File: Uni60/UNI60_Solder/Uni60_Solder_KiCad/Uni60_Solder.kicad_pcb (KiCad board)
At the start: 2 copper layers, 284.7 x 94.2 mm, 195 parts, among them J1 Conn_01x04, SW1 SW_Push, SW2 SW_Push, U1 STM32F072CBTx, U2 XC6206PxxxMR, U3 USBLC6-2SC6

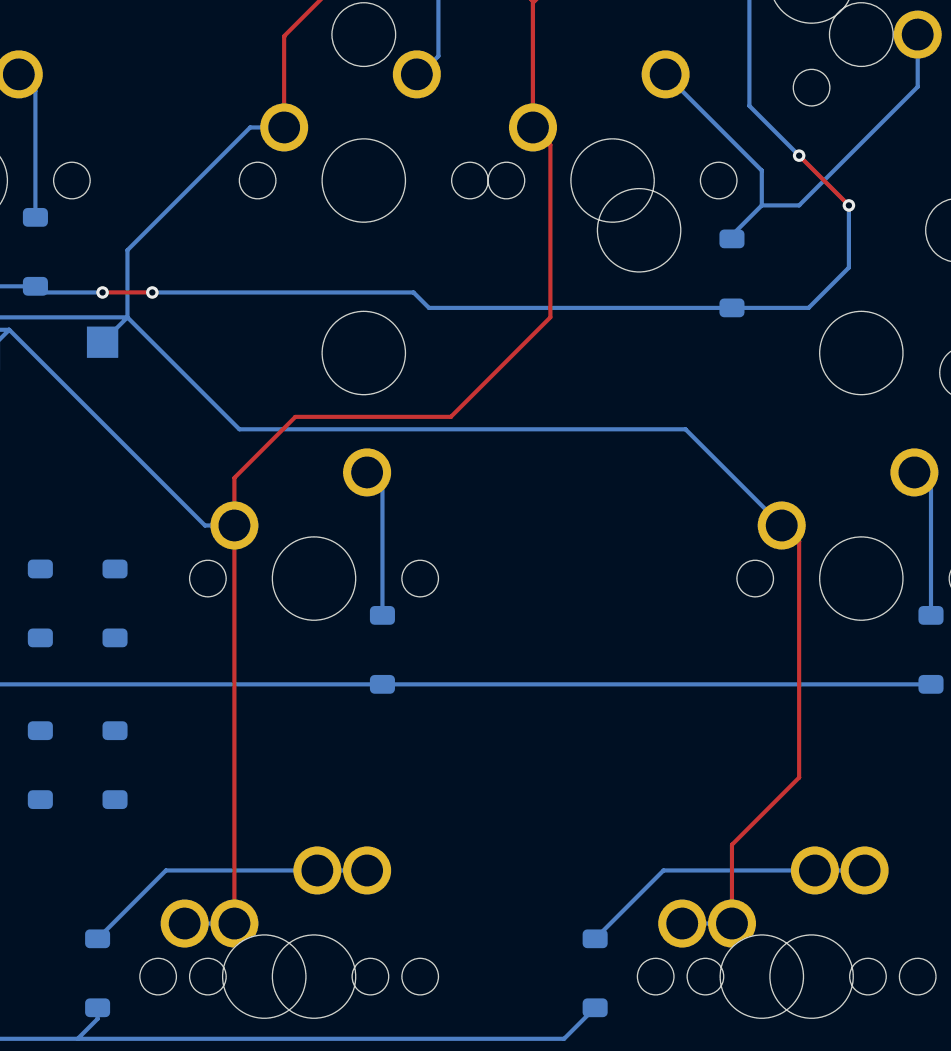
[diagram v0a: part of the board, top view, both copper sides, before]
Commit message: aadded full 2.75u rshift support
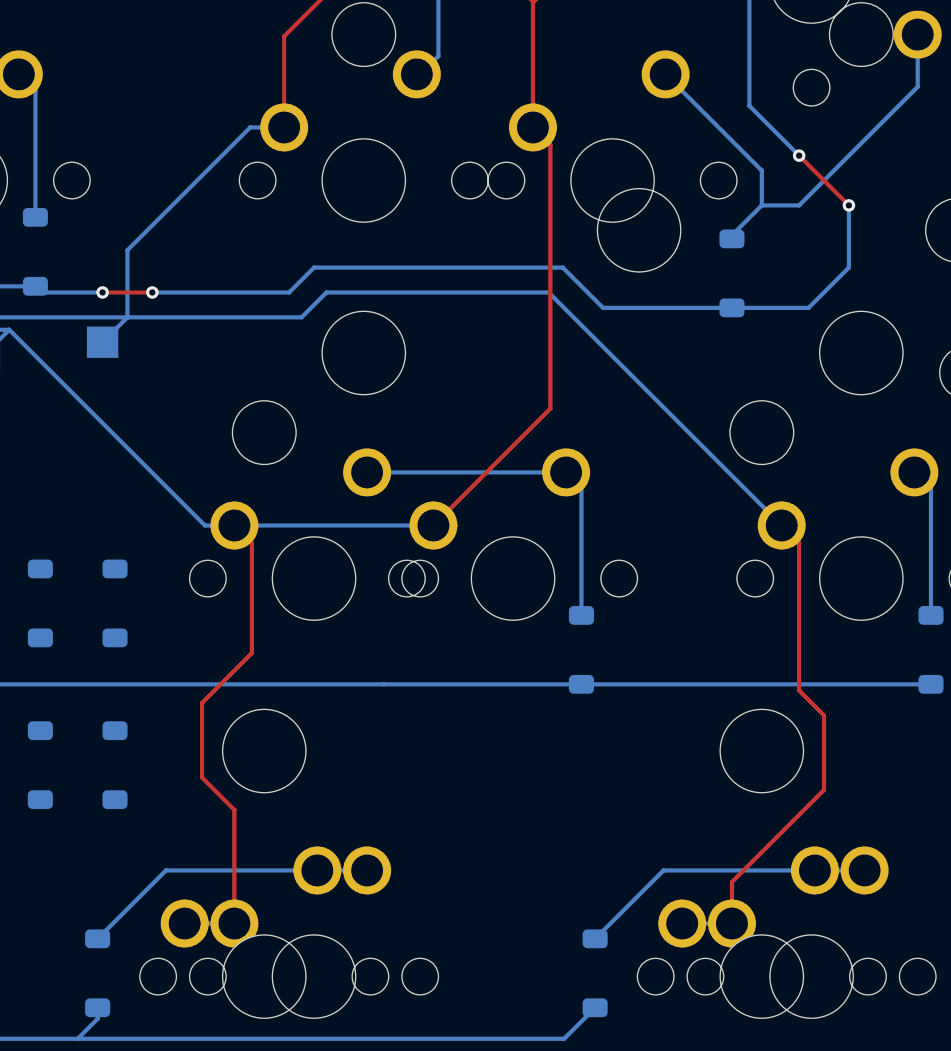
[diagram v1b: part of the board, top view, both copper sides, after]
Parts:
- added KC_RSFT_2.75u1: MX_SW_solder, shentobento:SW_MX_1u, F.Cu at (331.0, 135.6)
- added REF**: STAB_MX_2.75u, shentobento:STAB_MX_2.75u, F.Cu at (331.0, 135.6)
- moved D54 9.53 mm to (334.3, 139.0)
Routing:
- net Net-(D54-A): track 7.15 -> 16.7 mm
- net /COL12: track 351.7 -> 354.8 mm
- net /COL13: track 364.1 -> 366.0 mm
- net /ROW2: track 318.5 -> 319.5 mm

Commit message: moved jst to venom60he jst position
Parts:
- moved GND1 38.3 mm to (91.2, 126.0)
- moved U3 22.2 mm to (90.8, 85.4), turned to 90 degrees
- moved J1 22.1 mm to (97.0, 89.6)
- moved C8 6.55 mm to (89.7, 95.6), turned to -90 degrees
- moved C7 5.32 mm to (93.5, 92.4)
- moved U2 5.32 mm to (92.0, 93.9)
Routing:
- net +5V: track 30.5 -> 16.5 mm, vias 2 -> 4
- net /ROW0: track 285.9 -> 276.0 mm, vias 0 -> 2
- net /ESD_D+: track 23.3 -> 32.1 mm
- net /USB_D+: track 3.20 -> 7.75 mm
- net /ESD_D-: track 24.8 -> 27.8 mm
- net +3.3V: track 72.0 -> 69.8 mm
- net /USB_D-: track 3.22 -> 5.15 mm

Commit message: idk what changed tbh
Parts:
- added J2: Conn_01x04, shentobento:JST_SH_1x04, B.Cu at (76.2, 106.7)
- added J3: Conn_01x04, shentobento:JST_SH_1x04, B.Cu at (140.3, 107.9)
- added J4: Conn_01x04, shentobento:JST_SH_1x04, B.Cu at (119.4, 89.6)
- moved COL2 15.2 mm to (114.6, 105.2)
- moved U3 15.2 mm to (101.8, 95.8), turned to -90 degrees
- moved C7 11.4 mm to (99.9, 101.8), turned to 0 degrees
- moved U2 9.31 mm to (98.1, 100.9), turned to 0 degrees
- moved COL3 9.09 mm to (138.7, 99.3)
- moved SW2 7.63 mm to (130.4, 107.9)
- moved SW1 7.63 mm to (124.7, 107.9)
- moved C8 7.19 mm to (95.0, 100.4), turned to 90 degrees
- moved GND1 6.42 mm to (97.5, 125.2), turned to 0 degrees
- moved C6 4.39 mm to (93.8, 102.8), turned to -90 degrees
- moved COL13 2.40 mm to (313.7, 124.6)
- moved D72 0.89 mm to (262.4, 149.5)
- moved D3 0.44 mm to (122.3, 81.8)
- moved D29 0.16 mm to (91.7, 119.9)
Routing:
- net +5V: track 16.5 -> 113.5 mm, vias 4 -> 7
- net /USB_D-: track 5.15 -> 101.4 mm, vias 0 -> 3
- net /USB_D+: track 7.75 -> 99.4 mm, vias 0 -> 6
- net /ESD_D+: track 32.1 -> 7.21 mm
- net /ESD_D-: track 27.8 -> 6.63 mm
- net /ROW0: track 276.0 -> 295.7 mm, vias 2 -> 4
- net /COL1: track 116.0 -> 123.4 mm
- net /BOOT0: track 19.3 -> 23.5 mm, vias 0 -> 2
- net /COL2: track 120.4 -> 117.2 mm
- net +3.3V: track 69.8 -> 67.4 mm
- net /ROW2: track 319.5 -> 321.5 mm
- net GND: track 23.5 -> 24.7 mm, vias 33 -> 39
- net /COL0: track 124.6 -> 123.7 mm
- net /NRST: track 32.9 -> 33.5 mm, vias 4 -> 2
- net /COL3: track 161.8 -> 162.4 mm
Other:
- board text added: "+"
- board text added: "-"
- board text added: "0"
- board text added: "1"
- board text added: "1.25u LSHIFT"
- board text added: "1.25u/1.5u ALT"
- board text added: "1.25u/1.5u CTRL"
- board text added: "1.25u/1u GUI"
- board text added: "1.5u/1.25u ALT"
- board text added: "1.5u/1.25u CTRL"
- board text added: "1.75u RSHIFT"
- board text added: "1u/1.25u GUI"
- board text added: "2"
- board text added: "2.25u LSHIFT"
- board text added: "2.75u RSHIFT"
- board text added: "3"
- board text added: "4"
- board text added: "5"
- board text added: "6"
- board text added: "7"
- board text added: "8"
- board text added: "9"
- board text added: ":"
- board text added: "<"
- board text added: "<>"
- board text added: ">"
- board text added: "?"
- board text added: "A"
- board text added: "ANSI ENTER"
- board text added: "B"
- board text added: "BSPC"
- board text added: "Bakeneko"
- board text added: "C"
- board text added: "CAPS"
- board text added: "D"
- board text added: "E"
- board text added: "ESC"
- board text added: "F"
- board text added: "FN"
- board text added: "G"
- board text added: "H"
- board text added: "I"
- board text added: "ISO ENTER"
- board text added: "ISO \"
- board text added: "J"
- board text added: "K"
- board text added: "Keycult"
- board text added: "L"
- board text added: "M"
- board text added: "N"
- board text added: "O"
- board text added: "P"
- board text added: "Q"
- board text added: "R"
- board text added: "S"
- board text added: "STEP"
- board text added: "Standard"
- board text added: "T"
- board text added: "TAB"
- board text added: "U"
- board text added: "Uni60 v1.0 by ShentoBento"
- board text added: "Unikorn"
- board text added: "V"
- board text added: "W"
- board text added: "X"
- board text added: "Y"
- board text added: "Z"
- board text added: "\"
- board text added: "{"
- board text added: "{dblquote}"
- board text added: "}"
- board text removed: "ISO ENT"

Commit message: added stinga support
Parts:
- added J5: Conn_01x04, shentobento:JST_SH_1x04, B.Cu at (157.0, 85.0)
- added J6: Conn_01x04, Connector_Molex:Molex_Pico-EZmate_78171-0004_1x04-1MP_P1.20mm_Vertical, B.Cu at (137.7, 89.6)
- moved D5 5.91 mm to (165.0, 78.0)
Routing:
- net +5V: track 113.5 -> 160.8 mm, vias 7 -> 5
- net /USB_D-: track 101.4 -> 148.1 mm, vias 3 -> 2
- net /USB_D+: track 99.4 -> 145.8 mm, vias 6 -> 5
- net /ROW0: track 295.7 -> 307.6 mm, vias 4 -> 6
- net GND: track 24.7 -> 27.3 mm, vias 39 -> 41
- net Net-(D5-A): track 7.17 -> 6.49 mm
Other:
- outline, holes or cut-outs redrawn
- board text added: "Stinga"
